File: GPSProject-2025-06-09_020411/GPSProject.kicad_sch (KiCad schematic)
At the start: 12 parts, among them J1 USB_B_Micro, SW1 SW_Push, SW2 SW_Push, U1 ESP32-C3-WROOM-02, U2 CH340C, U3 SIM800L, U4 L76L-M33

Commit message: changed file
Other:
- note added: "hoi"
- moved on the sheet: U4
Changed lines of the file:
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@@
+		)
+	)
+	(text "hoi"
+		(exclude_from_sim no)
+		(at 152.908 98.044 0)
+		(effects
+			(font
+				(size 1.27 1.27)
+			)
 		)
 	)
@@
 	(symbol
 		(lib_id "L76L-M33:L76L-M33")
-		(at 102.87 160.02 0)
+		(at 109.22 158.75 0)
 		(unit 1)
 		(exclude_from_sim no)
@@
 		(fields_autoplaced yes)
 		(property "Reference" "U4"
-			(at 102.87 137.16 0)
+			(at 109.22 135.89 0)
 			(effects
 				(font
@@
 		)
 		(property "Value" "L76L-M33"
-			(at 102.87 139.7 0)
+			(at 109.22 138.43 0)
 			(effects
 				(font
@@
 		)
 		(property "Footprint" "L76L-M33:XCVR_L76L-M33"
-			(at 102.87 160.02 0)
+			(at 109.22 158.75 0)
 			(effects
 				(font
@@
 		)
 		(property "Datasheet" ""
-			(at 102.87 160.02 0)
+			(at 109.22 158.75 0)
 			(effects
 				(font
@@
 		)
 		(property "Description" ""
-			(at 102.87 160.02 0)
+			(at 109.22 158.75 0)
 			(effects
 				(font
@@
 		)
 		(property "MF" "Quectel"
-			(at 102.87 160.02 0)
+			(at 109.22 158.75 0)
 			(effects
 				(font
@@
 		)
 		(property "Description_1" "Navigation BeiDou, Galileo, GLONASS, GPS, GNSS Transceiver Module 1.561GHz, 1.575GHz, 1.602GHz Antenna Not Included Surface Mount"
-			(at 102.87 160.02 0)
+			(at 109.22 158.75 0)
 			(effects
 				(font
@@
 		)
 		(property "Package" "Custom Quectel"
-			(at 102.87 160.02 0)
+			(at 109.22 158.75 0)
 			(effects
 				(font
@@
 		)
 		(property "Price" "None"
-			(at 102.87 160.02 0)
+			(at 109.22 158.75 0)
 			(effects
 				(font
@@
 		)
 		(property "SnapEDA_Link" "https://www.snapeda.com/parts/L76LM33/Quectel/view-part/?ref=snap"
-			(at 102.87 160.02 0)
+			(at 109.22 158.75 0)
 			(effects
 				(font
@@
 		)
 		(property "MP" "L76LM33"
-			(at 102.87 160.02 0)
+			(at 109.22 158.75 0)
 			(effects
 				(font
@@
 		)
 		(property "Availability" "In Stock"
-			(at 102.87 160.02 0)
+			(at 109.22 158.75 0)
 			(effects
 				(font
@@
 		)
 		(property "Check_prices" "https://www.snapeda.com/parts/L76LM33/Quectel/view-part/?ref=eda"
-			(at 102.87 160.02 0)
-			(effects
-				(font
+			(at 109.22 158.75 0)
+			(effects
+				(font

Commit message: a
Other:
- note removed: "hoi"
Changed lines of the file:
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@@
-		)
-	)
-	(text "hoi"
-		(exclude_from_sim no)
-		(at 152.908 98.044 0)
-		(effects
-			(font
-				(size 1.27 1.27)
-			)
 		)
 	)

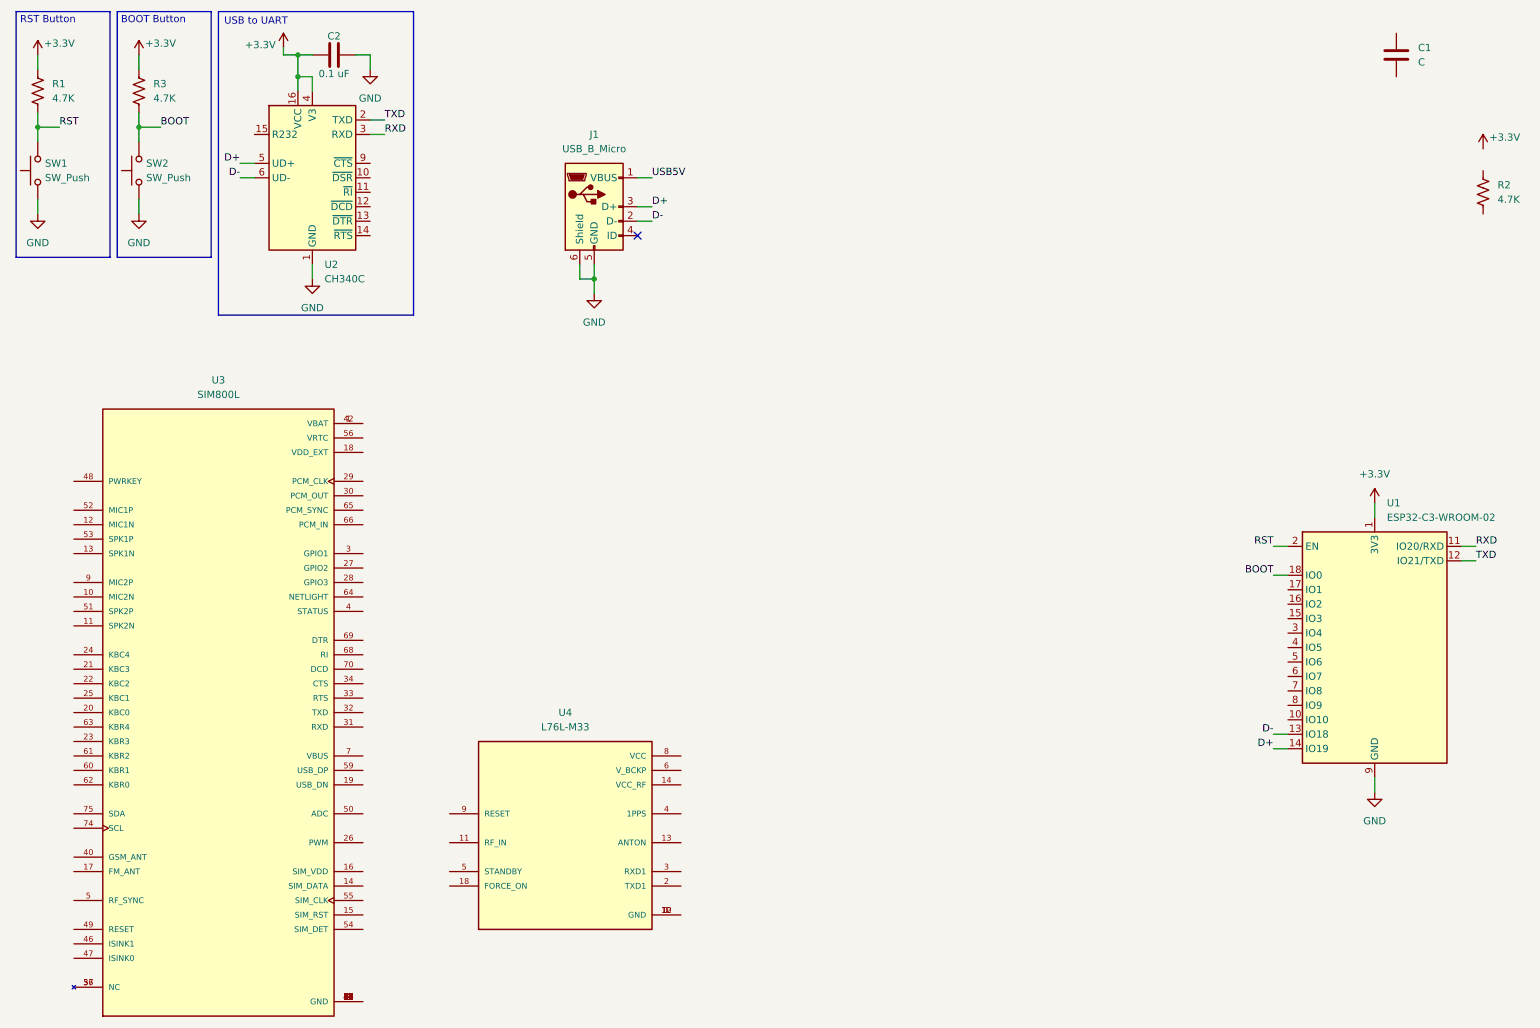
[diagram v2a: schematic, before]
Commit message: 6/14/25
- Added esp32-c3
- Added 18650 (Battery)
- Added TP4056 (Charger)
- Added Red and Green LED (For Battery & Charging)
- Added 1st iteration of "Battery & Charging" section

Notes:
- Check & Fix "Battery & Charging" connections
- Remove ESP32-C3-WROOM-02 & reconnect to ESP32-C3
- Remove "USB to UART" as not needed

To-Do's
- Do pins for other sections
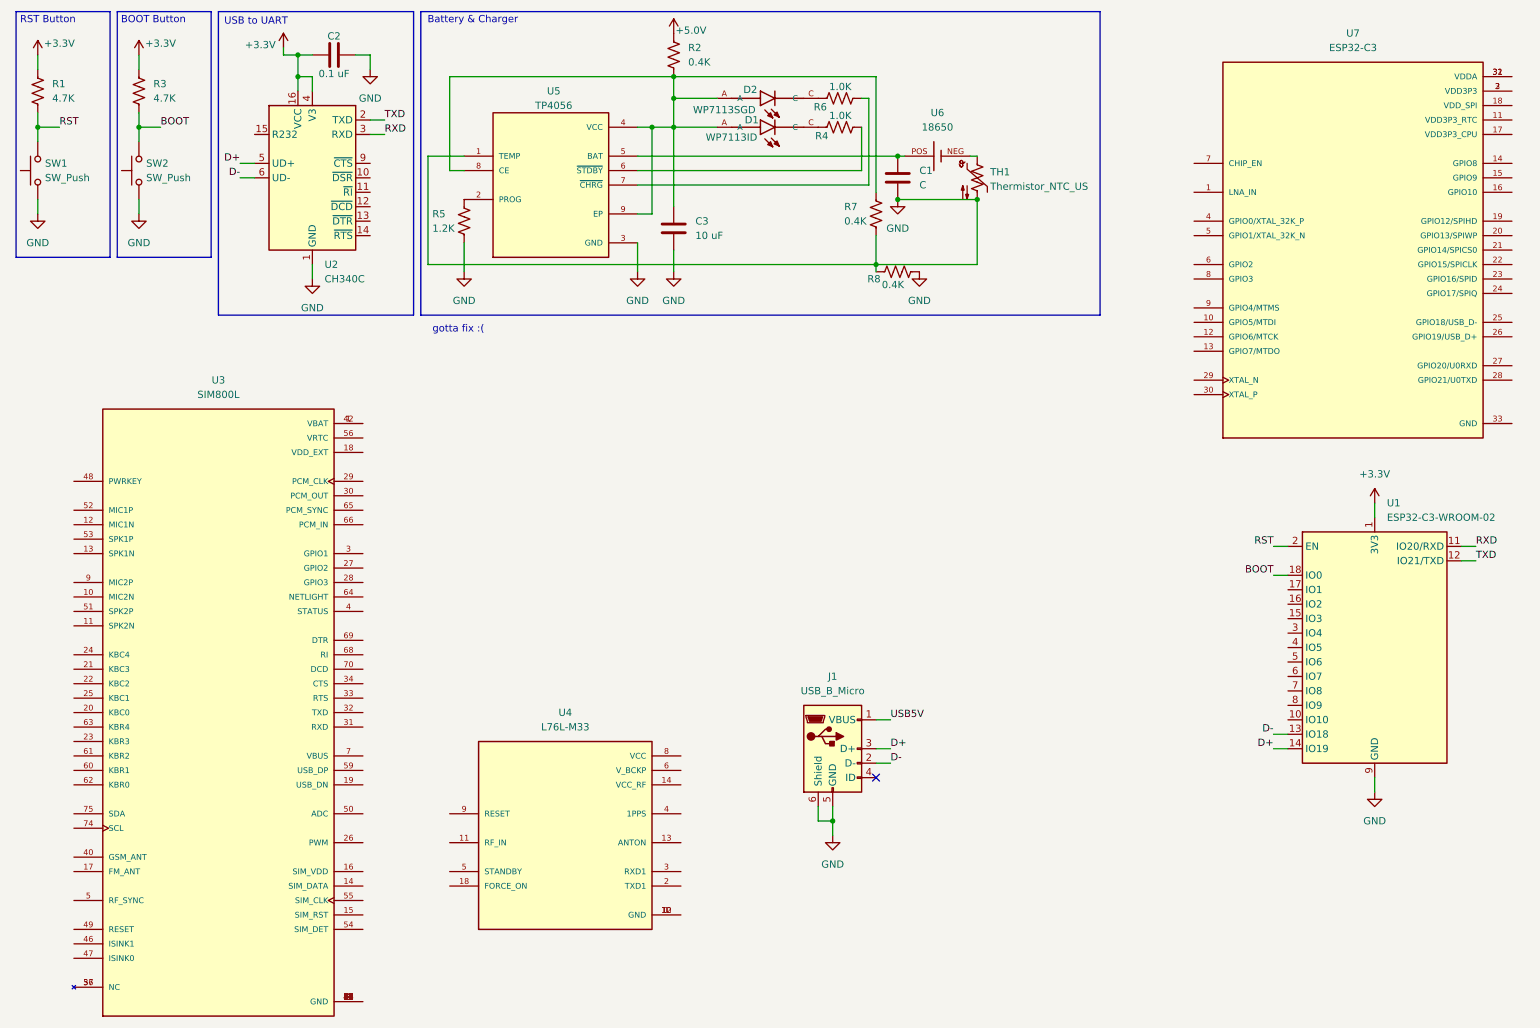
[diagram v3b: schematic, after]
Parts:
- added C3: 10 uF, symbol Device:C
- added D1: WP7113ID, WP7113ID:LED_WP7113ID, symbol WP7113ID:WP7113ID
- added D2: WP7113SGD, WP7113SGD:LED_WP7113SGD, symbol WP7113SGD:WP7113SGD
- added R4, R6: 1.0K, symbol Device:R_US
- added R5: 1.2K, symbol Device:R_US
- added R7, R8: 0.4K, symbol Device:R_US
- added TH1: Thermistor_NTC_US, symbol Device:Thermistor_NTC_US
- added U5: TP4056, TP4056:SOP127P600X175-9N, symbol TP4056:TP4056
- added U6: 18650, symbol 18650:18650
- added U7: ESP32-C3, ESP32-C3:QFN50P500X500X90-33N, symbol ESP32-C3:ESP32-C3
- R2: value 4.7K -> 0.4K
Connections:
- net GND: now also C1.2, C3.2, R5.2, R7.2, R8.1, R8.2, TH1.2, U5.1 (TEMP), U5.3 (GND)
- net +5.0V: now reaches R2.1
- net at R2.2: now also C3.1, D1.A, D2.A, R7.1, U5.4 (VCC), U5.8 (CE), U5.9 (EP)
- net at C1.1: now also U5.5 (BAT), U6.POS
- new net: U7.2 (VDD3P3), U7.3 (VDD3P3)
- new net: U7.31 (VDDA), U7.32 (VDDA)
- new net: D2.C, R6.1
- new net: R6.2, U5.7 (~{CHRG})
- new net: R5.1, U5.2 (PROG)
- new net: R4.2, U5.6 (~{STDBY})
- new net: D1.C, R4.1
- new net: TH1.1, U6.NEG
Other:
- note added: "Battery & Charger"
- note added: "gotta fix :("
- moved on the sheet: J1
